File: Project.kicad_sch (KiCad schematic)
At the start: 17 parts, among them P1 USB_C_Plug, SW1 DOUBLE_KEY, U1 MAX15062A, U2 TUSB8041, Y1 24MHz

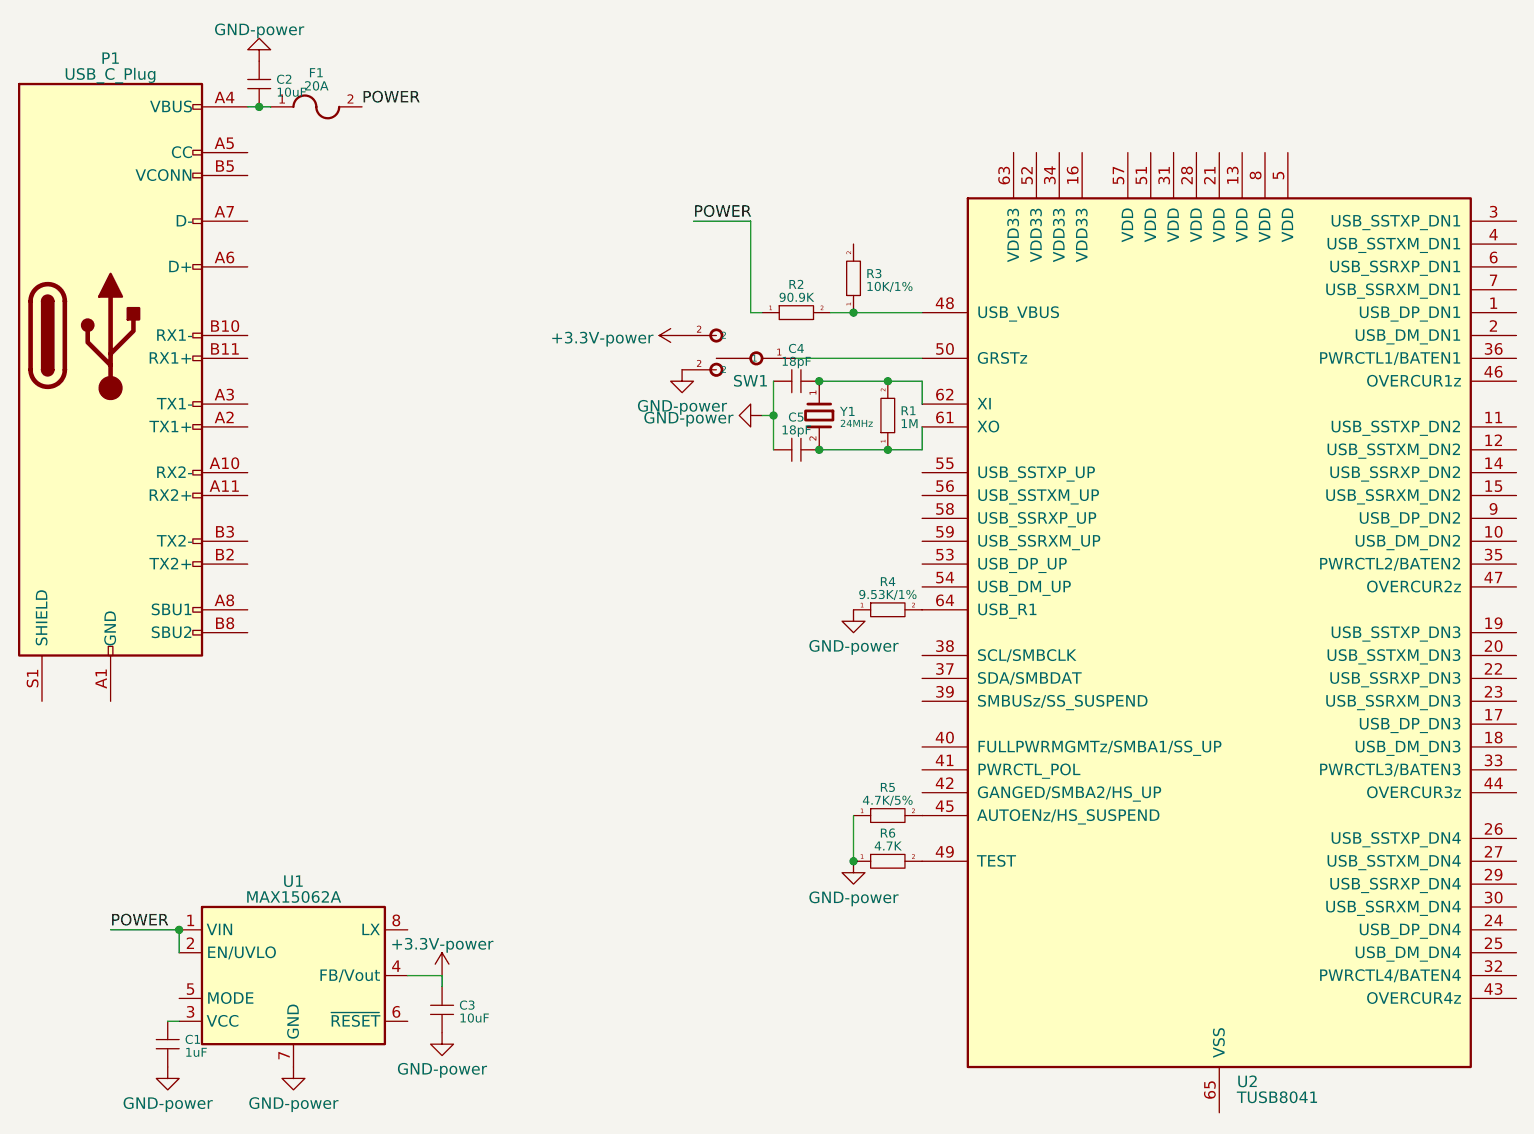
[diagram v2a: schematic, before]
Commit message: 完成USB上游设计
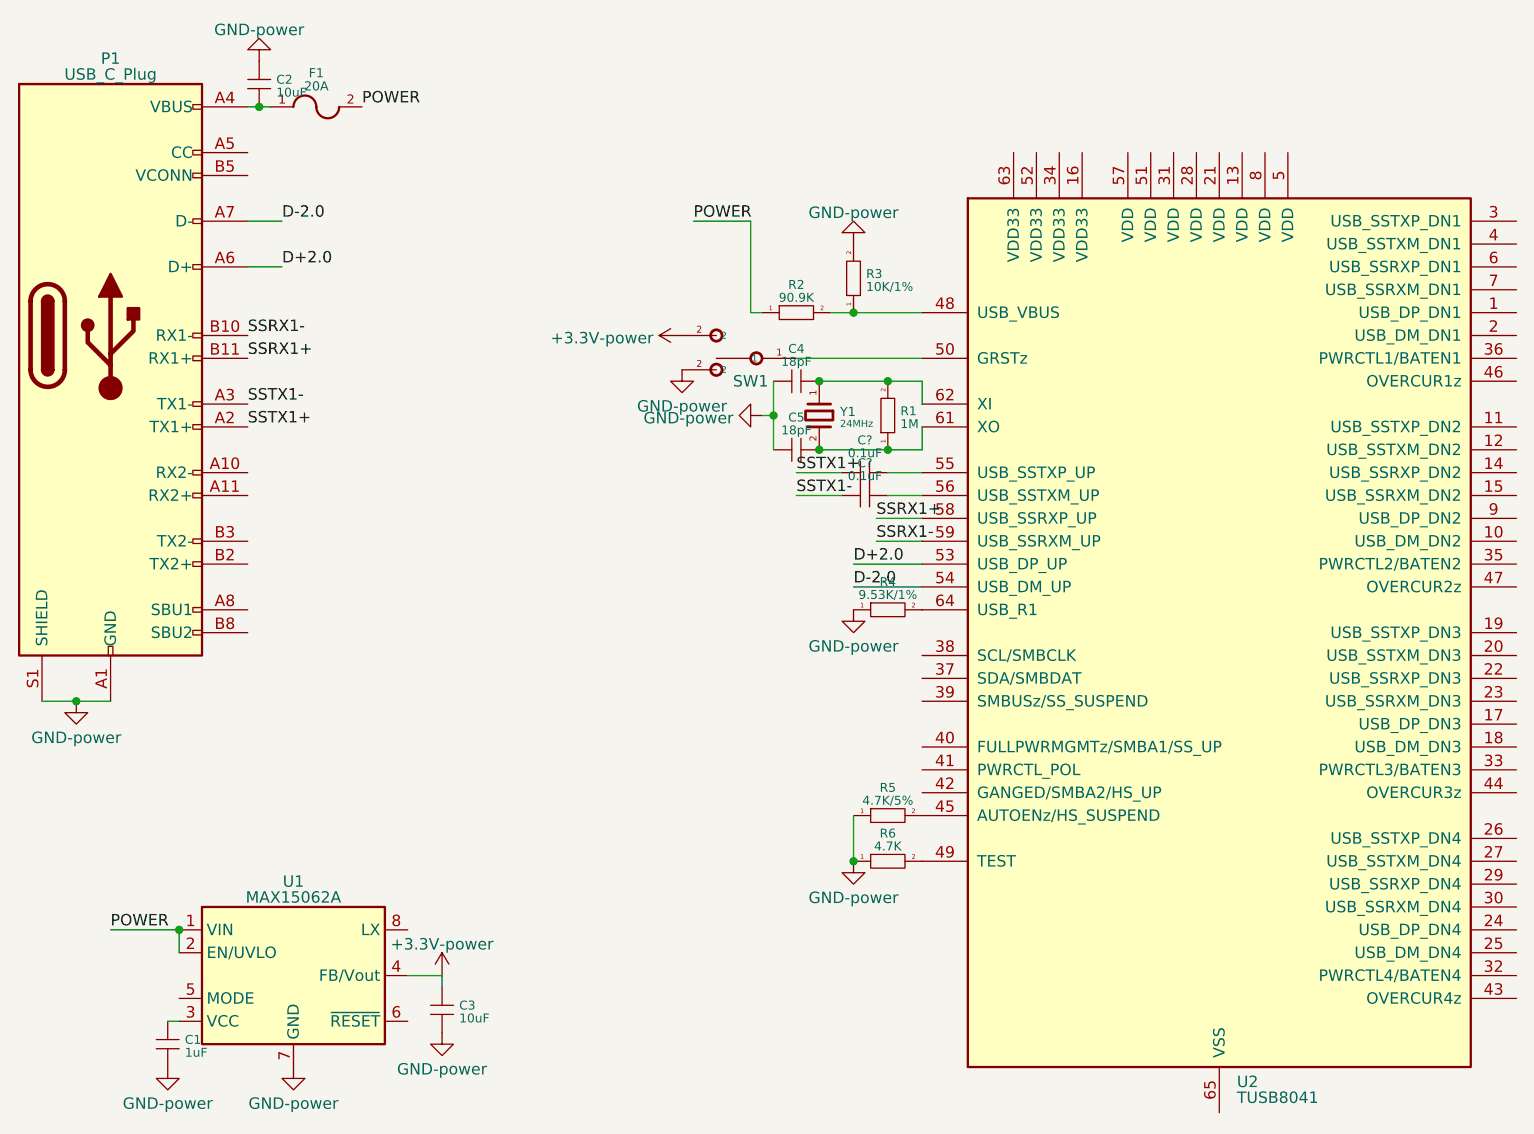
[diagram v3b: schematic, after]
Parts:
- added C? (x2): 0.1uF, symbol Lib1:C(MM)-LibCool
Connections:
- net GND: now also P1.A1 (GND), P1.A12 (GND), P1.B1 (GND), P1.B12 (GND), P1.S1 (SHIELD), R3.2
- net SSTX1+: now reaches P1.A2 (TX1+)
- net SSTX1+: now also C?.1
- net SSTX1-: now reaches P1.A3 (TX1-)
- net SSTX1-: now also C?.1
- net D+2.0: now reaches P1.A6 (D+)
- net D+2.0: now also U2.53 (USB_DP_UP)
- net D-2.0: now reaches P1.A7 (D-)
- net D-2.0: now also U2.54 (USB_DM_UP)
- net SSRX1-: now reaches P1.B10 (RX1-)
- net SSRX1-: now also U2.59 (USB_SSRXM_UP)
- net SSRX1+: now reaches P1.B11 (RX1+)
- net SSRX1+: now also U2.58 (USB_SSRXP_UP)
- net at U2.55 (USB_SSTXP_UP): now also C?.2
- net at U2.56 (USB_SSTXM_UP): now also C?.2
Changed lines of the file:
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@@
   (junction (at 35.56 111.76) (diameter 0) (color 0 0 0 0)
   )
+  (junction (at 24.13 86.36) (diameter 0) (color 0 0 0 0)
+  )
   (junction (at 114.3 50.8) (diameter 0) (color 0 0 0 0)
   )
@@
     (stroke (width 0) (type default))
   )
+  (wire (pts (xy 113.03 68.58) (xy 118.11 68.58))
+    (stroke (width 0) (type default))
+  )
   (wire (pts (xy 43.18 20.32) (xy 44.45 20.32))
     (stroke (width 0) (type default))
   )
+  (wire (pts (xy 114.3 63.5) (xy 118.11 63.5))
+    (stroke (width 0) (type default))
+  )
+  (wire (pts (xy 104.14 63.5) (xy 109.22 63.5))
+    (stroke (width 0) (type default))
+  )
   (wire (pts (xy 60.96 116.84) (xy 64.77 116.84))
     (stroke (width 0) (type default))
@@
     (stroke (width 0) (type default))
   )
+  (wire (pts (xy 114.3 60.96) (xy 118.11 60.96))
+    (stroke (width 0) (type default))
+  )
   (wire (pts (xy 99.06 33.02) (xy 99.06 43.18))
     (stroke (width 0) (type default))
   )
+  (wire (pts (xy 24.13 86.36) (xy 27.94 86.36))
+    (stroke (width 0) (type default))
+  )
+  (wire (pts (xy 110.49 71.12) (xy 118.11 71.12))
+    (stroke (width 0) (type default))
+  )
   (wire (pts (xy 101.6 54.61) (xy 101.6 58.42))
     (stroke (width 0) (type default))
@@
     (stroke (width 0) (type default))
   )
+  (wire (pts (xy 20.32 86.36) (xy 24.13 86.36))
+    (stroke (width 0) (type default))
+  )
   (wire (pts (xy 35.56 111.76) (xy 35.56 114.3))
     (stroke (width 0) (type default))
@@
     (stroke (width 0) (type default))
   )
+  (wire (pts (xy 43.18 38.1) (xy 46.99 38.1))
+    (stroke (width 0) (type default))
+  )
   (wire (pts (xy 101.6 50.8) (xy 101.6 54.61))
     (stroke (width 0) (type default))
   )
+  (wire (pts (xy 104.14 60.96) (xy 109.22 60.96))
+    (stroke (width 0) (type default))
+  )
   (wire (pts (xy 44.45 20.32) (xy 45.72 20.32))
     (stroke (width 0) (type default))
@@
     (stroke (width 0) (type default))
   )
+  (wire (pts (xy 113.03 66.04) (xy 118.11 66.04))
+    (stroke (width 0) (type default))
+  )
   (wire (pts (xy 110.49 99.06) (xy 110.49 104.14))
     (stroke (width 0) (type default))
@@
     (stroke (width 0) (type default))
   )
+  (wire (pts (xy 110.49 73.66) (xy 118.11 73.66))
+    (stroke (width 0) (type default))
+  )
+  (wire (pts (xy 43.18 33.02) (xy 46.99 33.02))
+    (stroke (width 0) (type default))
+  )
   (label "POWER" (at 92.71 33.02 0) (fields_autoplaced)
     (effects (font (size 1.27 1.27)) (justify left bottom))
   )
+  (label "D+2.0" (at 110.49 71.12 0) (fields_autoplaced)
+    (effects (font (size 1.27 1.27)) (justify left bottom))
+  )
+  (label "SSTX1+" (at 104.14 60.96 0) (fields_autoplaced)
+    (effects (font (size 1.27 1.27)) (justify left bottom))
+  )
+  (label "D-2.0" (at 110.49 73.66 0) (fields_autoplaced)
+    (effects (font (size 1.27 1.27)) (justify left bottom))
+  )
+  (label "SSTX1-" (at 43.18 53.34 0) (fields_autoplaced)
+    (effects (font (size 1.27 1.27)) (justify left bottom))
+  )
+  (label "SSRX1+" (at 113.03 66.04 0) (fields_autoplaced)
+    (effects (font (size 1.27 1.27)) (justify left bottom))
+  )
+  (label "SSRX1+" (at 43.18 48.26 0) (fields_autoplaced)
+    (effects (font (size 1.27 1.27)) (justify left bottom))
+  )
   (label "POWER" (at 55.88 20.32 0) (fields_autoplaced)
     (effects (font (size 1.27 1.27)) (justify left bottom))
   )
+  (label "SSTX1+" (at 43.18 55.88 0) (fields_autoplaced)
+    (effects (font (size 1.27 1.27)) (justify left bottom))
+  )
+  (label "SSRX1-" (at 43.18 45.72 0) (fields_autoplaced)
+    (effects (font (size 1.27 1.27)) (justify left bottom))
+  )
   (label "POWER" (at 27.94 111.76 0) (fields_autoplaced)
     (effects (font (size 1.27 1.27)) (justify left bottom))
   )
+  (label "SSTX1-" (at 104.14 63.5 0) (fields_autoplaced)
+    (effects (font (size 1.27 1.27)) (justify left bottom))
+  )
+  (label "D-2.0" (at 46.99 33.02 0) (fields_autoplaced)
+    (effects (font (size 1.27 1.27)) (justify left bottom))
+  )
+  (label "SSRX1-" (at 113.03 68.58 0) (fields_autoplaced)
+    (effects (font (size 1.27 1.27)) (justify left bottom))
+  )
+  (label "D+2.0" (at 46.99 38.1 0) (fields_autoplaced)
+    (effects (font (size 1.27 1.27)) (justify left bottom))
+  )
   (symbol (lib_id "Lib1:GND-power") (at 48.26 127 0) (unit 1)
     (in_bom yes) (on_board yes) (fields_autoplaced)
@@
     )
     (pin "1")
+  )
+  (symbol (lib_id "Lib1:C(MM)-LibCool") (at 111.76 60.96 0) (unit 1)
+    (in_bom yes) (on_board yes) (fields_autoplaced)
+    (property "Reference" "C?" (id 0) (at 111.76 57.3566 0)
+      (effects (font (size 0.9906 0.9906)))
+    )
+    (property "Value" "0.1uF" (id 1) (at 111.76 58.787 0)
+      (effects (font (size 0.9906 0.9906)))
+    )
+    (property "Footprint" "" (id 2) (at 112.7252 64.77 0)
+      (effects (font (size 0.762 0.762)))
+    )
+    (property "Datasheet" "" (id 3) (at 111.76 60.96 0)
+      (effects (font (size 1.524 1.524)))
+    )
+    (pin "1")
+    (pin "2")
   )
   (symbol (lib_id "Lib1:GND-power") (at 100.33 54.61 270) (unit 1)
@@
     )
     (pin "1")
+  )
+  (symbol (lib_id "Lib1:C(MM)-LibCool") (at 111.76 63.5 0) (unit 1)
+    (in_bom yes) (on_board yes) (fields_autoplaced)
+    (property "Reference" "C?" (id 0) (at 111.76 59.8966 0)
+      (effects (font (size 0.9906 0.9906)))
+    )
+    (property "Value" "0.1uF" (id 1) (at 111.76 61.327 0)
+      (effects (font (size 0.9906 0.9906)))
+    )
+    (property "Footprint" "" (id 2) (at 112.7252 67.31 0)
+      (effects (font (size 0.762 0.762)))
+    )
+    (property "Datasheet" "" (id 3) (at 111.76 63.5 0)
+      (effects (font (size 1.524 1.524)))
+    )
+    (pin "1")
+    (pin "2")
   )
   (symbol (lib_id "Lib1:FUSE*-LibCool") (at 50.8 20.32 0) (unit 1)
@@
     )
     (property "Datasheet" "" (id 3) (at 34.29 127 0)
+      (effects (font (size 1.27 1.27)) hide)
+    )
+    (pin "1")
+  )
+  (symbol (lib_id "Lib1:GND-power") (at 110.49 35.56 0) (mirror x) (unit 1)
+    (in_bom yes) (on_board yes) (fields_autoplaced)
+    (property "Reference" "#PWR?" (id 0) (at 110.49 29.21 0)
+      (effects (font (size 1.27 1.27)) hide)
+    )
+    (property "Value" "GND-power" (id 1) (at 110.49 32.0771 0)
+      (effects (font (size 1.27 1.27)))
+    )
+    (property "Footprint" "" (id 2) (at 110.49 35.56 0)
+      (effects (font (size 1.27 1.27)) hide)
+    )
+    (property "Datasheet" "" (id 3) (at 110.49 35.56 0)
       (effects (font (size 1.27 1.27)) hide)
     )
@@
     (pin "1")
   )
+  (symbol (lib_id "Lib1:GND-power") (at 24.13 86.36 0) (unit 1)
+    (in_bom yes) (on_board yes) (fields_autoplaced)
+    (property "Reference" "#PWR?" (id 0) (at 24.13 92.71 0)
+      (effects (font (size 1.27 1.27)) hide)
+    )
+    (property "Value" "GND-power" (id 1) (at 24.13 90.4161 0)
+      (effects (font (size 1.27 1.27)))
+    )
+    (property "Footprint" "" (id 2) (at 24.13 86.36 0)
+      (effects (font (size 1.27 1.27)) hide)
+    )
+    (property "Datasheet" "" (id 3) (at 24.13 86.36 0)
+      (effects (font (size 1.27 1.27)) hide)
+    )
+    (pin "1")
+  )
   (sheet_instances
     (path "/" (page "1"))
@@
       (reference "#PWR010") (unit 1) (value "GND-power") (footprint "")
     )
+    (path "/43e62d3f-078a-46b5-9aad-3580113edb1c"
+      (reference "#PWR?") (unit 1) (value "GND-power") (footprint "")
+    )
+    (path "/e76b25d7-3715-4eb5-9a0b-e350314b8659"
+      (reference "#PWR?") (unit 1) (value "GND-power") (footprint "")
+    )
     (path "/1af607d6-b127-45ad-990a-6c742ba65adb"
       (reference "C1") (unit 1) (value "1uF") (footprint "")
@@
       (reference "C5") (unit 1) (value "18pF") (footprint "")
     )
+    (path "/086eefd6-9597-49ab-8616-01d18a11ff75"
+      (reference "C?") (unit 1) (value "0.1uF") (footprint "")
+    )
+    (path "/096465ef-f57e-435a-aa9a-0a2ca894761a"
+      (reference "C?") (unit 1) (value "0.1uF") (footprint "")
+    )
     (path "/0a2280bb-1e4e-4610-aa91-7ae5b887a75a"
